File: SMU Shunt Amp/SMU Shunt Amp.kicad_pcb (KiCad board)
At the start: 4 copper layers, 99.1 x 37.6 mm, 51 parts, among them J1 30VDC, J2 Input, J3 Output, U1 LT3088, U2 OPA189IDBVx, U3 THS4021CxDGNx, U4 TLE2426xD, U5 OPA1611AIDR

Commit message: PCB layout initial.
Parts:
- removed C10, C14, C15: 10u, Capacitor_SMD:CP_Elec_6.3x7.7
- removed C11: 1u, Capacitor_SMD:C_0805_2012Metric_Pad1.18x1.45mm_HandSolder
- removed C12, C13: Optional, Capacitor_SMD:C_0805_2012Metric_Pad1.18x1.45mm_HandSolder
- removed JP1: Term, Connector_PinHeader_2.54mm:PinHeader_1x02_P2.54mm_Vertical
- removed JP2: SIG, Connector_PinHeader_2.54mm:PinHeader_1x02_P2.54mm_Vertical
- removed JP3: 100uV, Connector_PinHeader_2.54mm:PinHeader_1x02_P2.54mm_Vertical
- removed JP4: GND, Connector_PinHeader_2.54mm:PinHeader_1x02_P2.54mm_Vertical
- removed R10: 1M, Resistor_SMD:R_0805_2012Metric_Pad1.20x1.40mm_HandSolder
- removed R11: 56K, Resistor_SMD:R_0805_2012Metric_Pad1.20x1.40mm_HandSolder
- removed R12: 1.47K, Resistor_SMD:R_0805_2012Metric_Pad1.20x1.40mm_HandSolder
- removed R13: 0R, Resistor_SMD:R_0805_2012Metric_Pad1.20x1.40mm_HandSolder
- removed R14: 49.9, Resistor_SMD:R_0805_2012Metric_Pad1.20x1.40mm_HandSolder
- removed R15: 1K, Resistor_SMD:R_0805_2012Metric_Pad1.20x1.40mm_HandSolder
- removed TP1: 100uV, TestPoint:TestPoint_Keystone_5010-5014_Multipurpose
- removed TP2: +14V, TestPoint:TestPoint_Keystone_5010-5014_Multipurpose
- removed TP3: -14V, TestPoint:TestPoint_Keystone_5010-5014_Multipurpose
- removed TP4: GND, TestPoint:TestPoint_Keystone_5010-5014_Multipurpose
- removed U3: THS4021CxDGNx, Package_SO:MSOP-8-1EP_3x3mm_P0.65mm_EP1.73x1.85mm_ThermalVias
- removed U4: TLE2426xD, Package_SO:SOIC-8_3.9x4.9mm_P1.27mm
- removed U5: OPA1611AIDR, Package_SO:SOIC-8_3.9x4.9mm_P1.27mm
- added D2: MBRA340, Diode_SMD:D_SMA_Handsoldering, F.Cu at (111.2, 39.9)
- added D3: Vz=30, Diode_SMD:D_SOD-123, F.Cu at (116.0, 50.3)
- C1, C2, C3, C4, R1: moved to B.Cu
- C5, C6: value 100n -> 10u; footprint Capacitor_SMD:C_0805_2012Metric_Pad1.18x1.45mm_HandSolder -> Capacitor_SMD:CP_Elec_6.3x7.7; moved to F.Cu
- C7: value 10u -> 715p; footprint Capacitor_SMD:CP_Elec_6.3x7.7 -> Capacitor_SMD:C_0805_2012Metric_Pad1.18x1.45mm_HandSolder; moved to B.Cu
- C8: value 10u -> Optional; footprint Capacitor_SMD:CP_Elec_6.3x7.7 -> Capacitor_SMD:C_0805_2012Metric_Pad1.18x1.45mm_HandSolder; moved to B.Cu
- C9: value 1u -> 6.8p; moved to B.Cu
- D1: value D -> MBRA340; footprint Diode_SMD:D_SOD-128 -> Diode_SMD:D_SMA_Handsoldering
- J1: footprint TerminalBlock_Phoenix:TerminalBlock_Phoenix_PT-1,5-2-5.0-H_1x02_P5.00mm_Horizontal -> TerminalBlock_Phoenix:TerminalBlock_Phoenix_PT-1,5-3-5.0-H_1x03_P5.00mm_Horizontal
- R2: value 1.54M -> 150R; moved to B.Cu
- R3: value 11R -> 14.7K; moved to B.Cu
- R4: value 560K -> 430R; moved to B.Cu
- R5: value 750R -> 14.7K; moved to B.Cu
- R6: value 0R -> 4.3K; moved to B.Cu
- R7: value 1.47K -> 60.4R; moved to B.Cu
- R8: value 15R -> 604R; moved to B.Cu
- R9: value 0R -> 49.9
- U1: value LT3088 -> OPA189IDBVx; footprint Package_TO_SOT_SMD:SOT-223 -> Package_TO_SOT_SMD:SOT-23-5_HandSoldering; moved to B.Cu
- U2: value OPA189IDBVx -> THS3092D; footprint Package_TO_SOT_SMD:SOT-23-5_HandSoldering -> Package_SO:SOIC-8_3.9x4.9mm_P1.27mm; moved to B.Cu
- moved C9 64.8 mm to (146.3, 47.5), turned to 180 degrees
- moved R5 63.3 mm to (146.3, 49.9)
- moved C7 55.6 mm to (142.9, 48.8), turned to 90 degrees
- moved R4 55.6 mm to (139.1, 55.0)
- moved U1 45.2 mm to (135.0, 52.5)
- moved D1 40.8 mm to (111.2, 60.9)
- moved J1 33.2 mm to (108.7, 45.5)
- moved H4 28.6 mm to (103.5, 65.3)
- moved H3 28.6 mm to (103.5, 35.9)
- moved C6 28.6 mm to (120.3, 43.7)
- moved R1 24.5 mm to (128.9, 51.4), turned to 90 degrees
- moved R2 21.4 mm to (137.8, 48.8), turned to 90 degrees
- moved R3 19.7 mm to (140.3, 48.8), turned to 90 degrees
- moved C5 18.1 mm to (120.3, 57.0), turned to 90 degrees
- moved R8 16.7 mm to (151.8, 53.7), turned to 90 degrees
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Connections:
- C7 pad 2: -15V -> GND
- C8 pad 2: GND -> Net-(C8-Pad2)
- C9 pad 2: -15V -> Net-(C7-Pad1)
- D1 pad 1: Net-(C7-Pad1) -> +15V
- J1 pad 1: Net-(D1-Pad2) -> Net-(D2-Pad1)
- J1 pad 2: -15V -> GND
- J2 pad 1: Net-(J2-Pad1) -> Net-(C8-Pad2)
- R1 pad 2: Net-(JP1-Pad1) -> Net-(C8-Pad2)
- R2 pad 1: +15V -> Net-(C7-Pad1)
- R2 pad 2: Net-(C8-Pad1) -> GND
- R3 pad 1: Net-(C8-Pad1) -> Net-(C7-Pad1)
- R4 pad 1: Net-(C9-Pad1) -> Net-(R4-Pad1)
- R4 pad 2: -15V -> Net-(C8-Pad1)
- R5 pad 1: +15V -> Net-(C9-Pad1)
- R5 pad 2: -15V -> Net-(C7-Pad1)
- R6 pad 1: Net-(C12-Pad2) -> Net-(R6-Pad1)
- R6 pad 2: Net-(C13-Pad1) -> Net-(R4-Pad1)
- R7 pad 1: Net-(C13-Pad1) -> Net-(R7-Pad1)
- R7 pad 2: GND -> Net-(R6-Pad1)
- R8 pad 1: Net-(C13-Pad1) -> Net-(C9-Pad1)
- R8 pad 2: GND -> Net-(R7-Pad1)
- R9 pad 1: Net-(R9-Pad1) -> Net-(J3-Pad1)
- R9 pad 2: Net-(C12-Pad1) -> Net-(C9-Pad1)
- U1 pad 1: Net-(C9-Pad1) -> Net-(C8-Pad1)
- U1 pad 2: +15V -> -15V
- U1 pad 3: Net-(C7-Pad1) -> Net-(C8-Pad2)
- U1 pad 4: +15V -> Net-(C7-Pad1)
- U2 pad 1: Net-(C12-Pad1) -> Net-(R6-Pad1)
- U2 pad 2: -15V -> Net-(R4-Pad1)
- U2 pad 3: Net-(JP2-Pad2) -> GND
- U2 pad 4: Net-(C12-Pad2) -> -15V
- U2 pad 5: +15V -> GND
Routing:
- net +15V: track 154.1 -> 56.0 mm, vias 4 -> 2
- net -15V: track 110.8 -> 56.0 mm, vias 4 -> 2
- net Net-(JP2-Pad2): track 30.3 -> 0.00 mm
- net NULLA: track 27.9 -> 0.00 mm
- net Net-(C13-Pad2): track 24.1 -> 0.00 mm, vias 1 -> 0
- net Net-(C7-Pad1): track 36.0 -> 12.4 mm
- net Net-(J2-Pad1): track 22.8 -> 0.00 mm
- net Net-(C12-Pad1): track 22.6 -> 0.00 mm, vias 1 -> 0
- net Net-(R6-Pad1): track 0.00 -> 15.0 mm, vias 0 -> 2
- net Net-(C13-Pad1): track 13.3 -> 0.00 mm
- net Net-(C8-Pad1): track 20.3 -> 10.4 mm
- net Net-(C9-Pad1): track 6.00 -> 15.1 mm
- net Net-(C8-Pad2): track 0.00 -> 8.14 mm
- net Net-(R4-Pad1): track 0.00 -> 5.82 mm
- net Net-(R7-Pad1): track 0.00 -> 5.73 mm
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- removed copper zone on In1.Cu, net (none)
- removed copper zone on In2.Cu, net (none)
- removed copper zone on F.Cu, net -15V
- removed copper zone on B.Cu, net Net-(U3-Pad9)
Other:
- board size 99.1 x 37.6 mm -> 69.9 x 37.6 mm
- board text added: "+"
- board text added: "-"
- board text added: "±15V MAX"
- board text added: "⏚"
- board text removed: "-V"
- board text removed: "30 VDC"
- board text removed: ">"

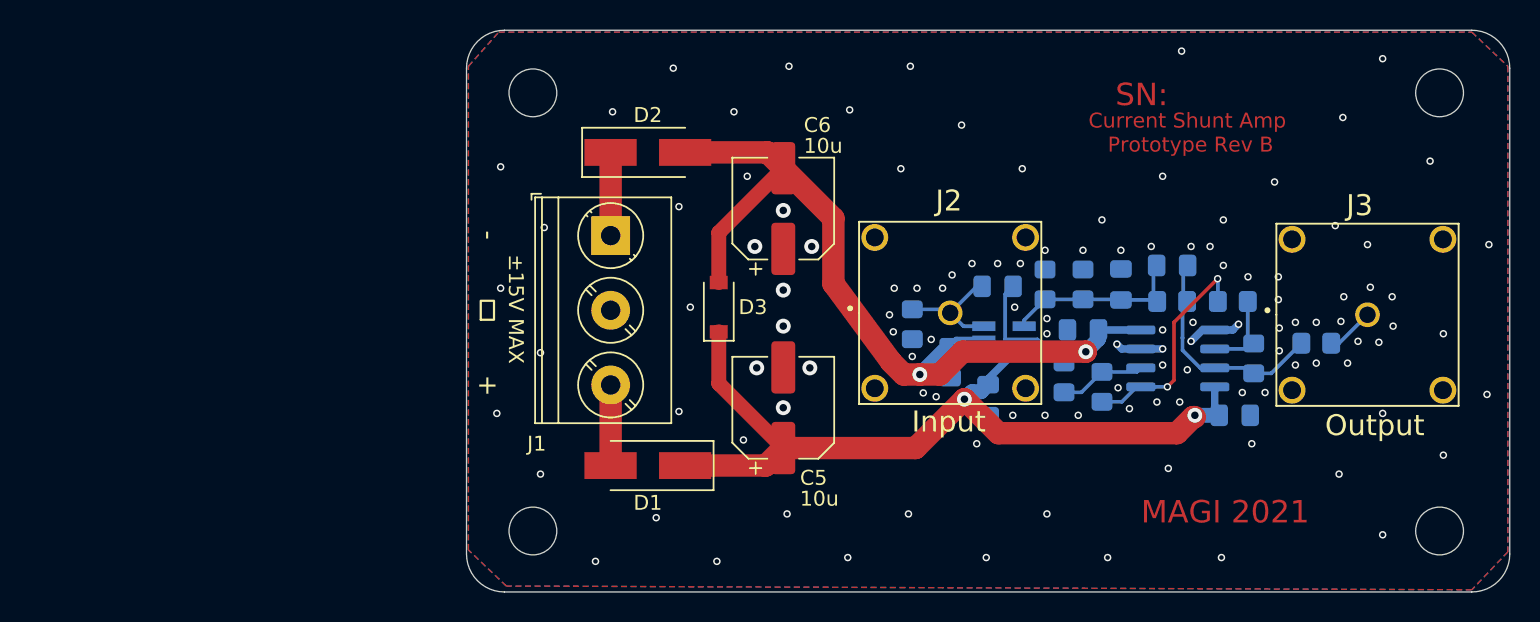
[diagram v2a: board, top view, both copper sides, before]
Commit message: More vias
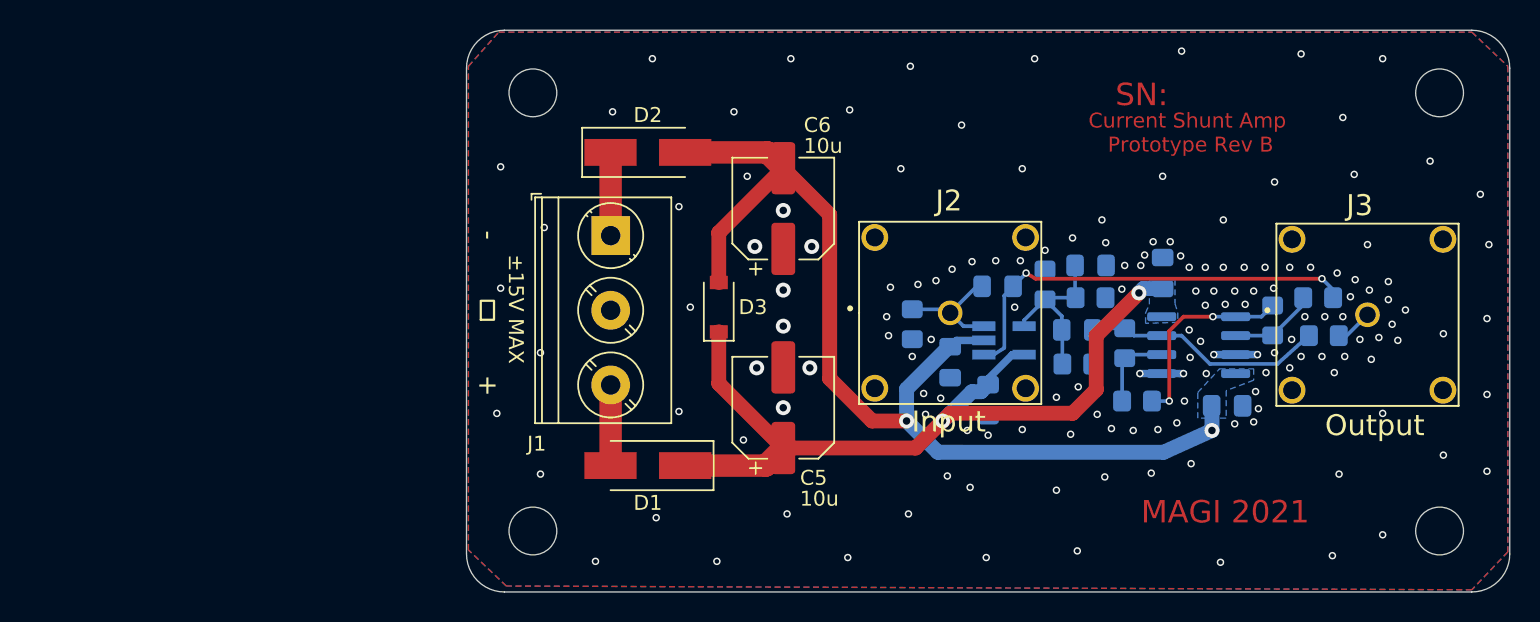
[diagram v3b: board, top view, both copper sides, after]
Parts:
- C8: value Optional -> 1u
- moved R4 17.8 mm to (156.1, 49.7), turned to 0 degrees
- moved R6 12.3 mm to (153.0, 51.2), turned to 270 degrees
- moved C2 10.9 mm to (150.0, 56.9), turned to 180 degrees
- moved C3 10.7 mm to (145.7, 48.0), turned to 90 degrees
- moved R7 9.25 mm to (144.0, 56.6), turned to 0 degrees
- moved R8 8.70 mm to (143.1, 52.7), turned to 270 degrees
- moved C9 7.68 mm to (140.0, 51.8)
- moved R5 7.61 mm to (140.0, 54.1)
- moved C7 2.40 mm to (140.8, 47.5), turned to 0 degrees
- moved U2 1.66 mm to (148.1, 52.8), turned to 180 degrees
- moved R3 1.02 mm to (140.8, 49.7), turned to 0 degrees
- moved R9 0.72 mm to (156.5, 52.2)
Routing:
- net Net-(C8-Pad1): track 10.4 -> 28.6 mm, vias 0 -> 2
- net -15V: track 56.0 -> 70.1 mm
- net Net-(C9-Pad1): track 15.1 -> 18.6 mm
- net Net-(R6-Pad1): track 15.0 -> 13.5 mm
- net GND: track 6.84 -> 5.84 mm, vias 115 -> 153
- net Net-(C7-Pad1): track 12.4 -> 11.5 mm
- net Net-(J3-Pad1): track 3.22 -> 2.50 mm
- added copper zone on B.Cu, net +15V
- added copper zone on B.Cu, net -15V

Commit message: Thicken output paths, add ferrites.
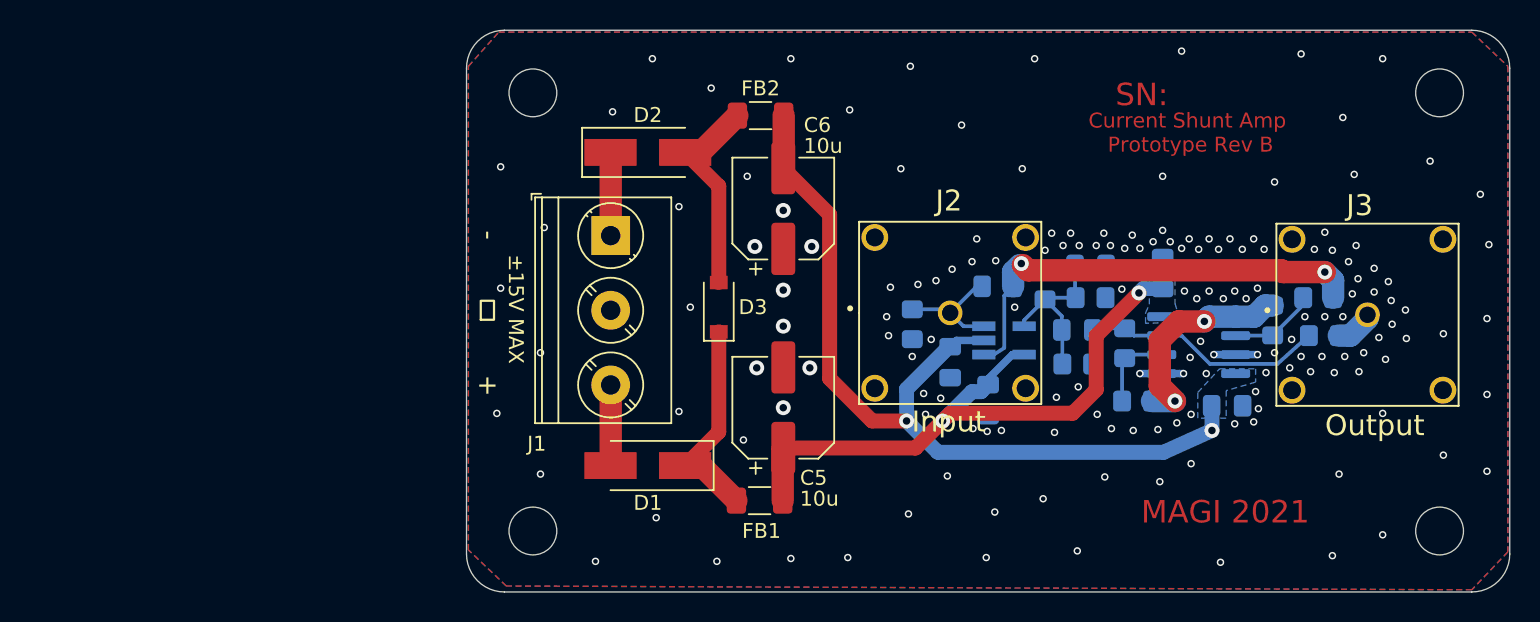
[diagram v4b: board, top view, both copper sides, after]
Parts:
- added FB1: 80R @ 100MHz, Resistor_SMD:R_1206_3216Metric_Pad1.30x1.75mm_HandSolder, F.Cu at (118.7, 63.2)
- added FB2: 80R @ 100MHz, Resistor_SMD:R_1206_3216Metric_Pad1.30x1.75mm_HandSolder, F.Cu at (118.7, 37.5)
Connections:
- D1 pad 1: +15V -> Net-(D1-Pad1)
- D2 pad 2: -15V -> Net-(D2-Pad2)
- D3 pad 1: +15V -> Net-(D1-Pad1)
- D3 pad 2: -15V -> Net-(D2-Pad2)
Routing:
- net Net-(D1-Pad1): track 0.00 -> 14.3 mm
- net Net-(D2-Pad2): track 0.00 -> 14.2 mm
- net +15V: track 56.1 -> 43.0 mm
- net -15V: track 70.1 -> 57.2 mm
- net Net-(C8-Pad1): track 28.6 -> 29.8 mm
- net Net-(R6-Pad1): track 13.5 -> 14.5 mm
- net GND: vias 153 -> 162

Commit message: New layout for better signal integrity
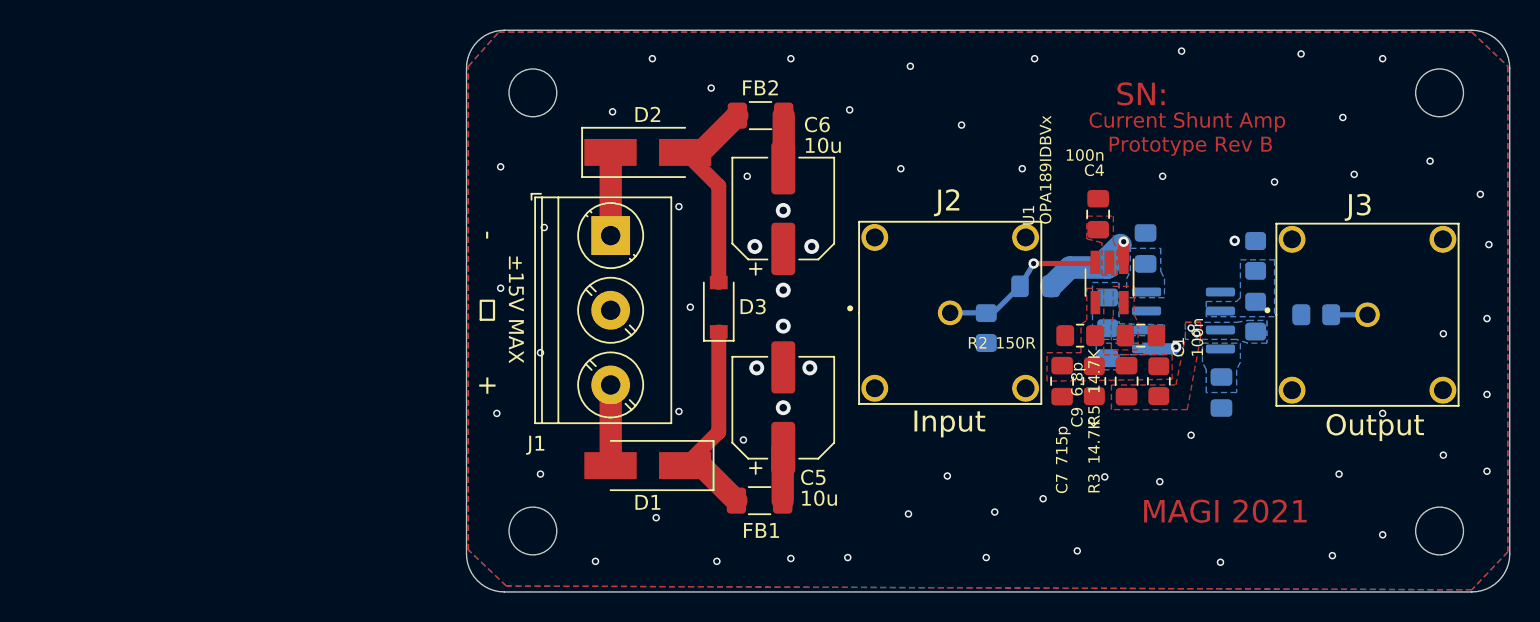
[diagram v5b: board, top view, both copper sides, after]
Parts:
- C1, C4, C7, C9, R2, R3, R5, U1: moved to F.Cu
- moved R4 14.1 mm to (142.0, 48.6), turned to 90 degrees
- moved C4 14.0 mm to (141.4, 44.1), turned to 270 degrees
- moved R7 12.5 mm to (151.9, 46.9), turned to 90 degrees
- moved C2 11.9 mm to (144.5, 46.4), turned to 270 degrees
- moved R6 11.2 mm to (142.0, 52.7), turned to 90 degrees
- moved C1 11.1 mm to (144.2, 52.2), turned to 0 degrees
- moved R8 8.94 mm to (151.9, 50.9), turned to 90 degrees
- moved C3 8.92 mm to (149.6, 56.0), turned to 270 degrees
- moved U1 8.06 mm to (142.1, 48.6), turned to 270 degrees
- moved C7 7.98 mm to (138.9, 55.2), turned to 270 degrees
- moved R3 5.59 mm to (141.1, 55.2), turned to 270 degrees
- moved R5 5.58 mm to (145.4, 55.2), turned to 90 degrees
- moved R1 4.96 mm to (133.9, 51.7)
- moved C9 4.76 mm to (143.3, 55.2), turned to 90 degrees
- moved R2 4.16 mm to (140.1, 52.2), turned to 180 degrees
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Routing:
- net -15V: track 57.2 -> 3.53 mm, vias 2 -> 1
- net +15V: track 43.0 -> 3.54 mm, vias 2 -> 0
- net Net-(C8-Pad1): track 29.8 -> 7.57 mm, vias 2 -> 1
- net Net-(C9-Pad1): track 18.6 -> 0.00 mm, vias 0 -> 2
- net Net-(R6-Pad1): track 14.5 -> 2.02 mm
- net Net-(C7-Pad1): track 11.5 -> 0.00 mm
- net Net-(R4-Pad1): track 5.86 -> 0.00 mm
- net GND: track 5.84 -> 0.00 mm, vias 162 -> 62
- net Net-(R7-Pad1): track 5.70 -> 0.00 mm
- net Net-(C8-Pad2): track 8.14 -> 11.4 mm, vias 0 -> 1
- added copper zone on F.Cu, net +15V
- added copper zone on F.Cu, net -15V
- added copper zone on F.Cu, net Net-(C7-Pad1)
- added copper zone on B.Cu, net Net-(C9-Pad1)
- added copper zone on F.Cu, net Net-(C9-Pad1)
- added copper zone on B.Cu, net Net-(R4-Pad1)
- added copper zone on B.Cu, net Net-(R6-Pad1)
- added copper zone on B.Cu, net Net-(R7-Pad1)

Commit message: Most routing done.
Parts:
- moved C1 3.89 mm to (147.4, 50.0)
- moved C2 2.69 mm to (147.1, 47.2), turned to 180 degrees
- moved C8 2.68 mm to (139.8, 48.6), turned to 270 degrees
- moved C4 1.52 mm to (142.9, 44.1)
- moved C7 1.52 mm to (140.5, 55.2)
- moved C9 1.52 mm to (144.8, 55.2)
- moved R2 1.52 mm to (141.7, 52.2)
- moved R3 1.52 mm to (142.6, 55.2)
- moved R5 1.52 mm to (146.9, 55.2)
- moved U1 1.52 mm to (143.6, 48.6)
- moved R1 1.14 mm to (134.4, 50.7)
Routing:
- net Net-(C8-Pad2): track 11.4 -> 0.00 mm, vias 1 -> 2
- net Net-(C9-Pad1): track 0.00 -> 11.2 mm
- net +15V: track 3.54 -> 13.8 mm, vias 0 -> 10
- net Net-(R6-Pad1): track 2.02 -> 10.6 mm, vias 2 -> 3
- net Net-(C8-Pad1): track 7.57 -> 1.34 mm, vias 1 -> 4
- net Net-(D2-Pad1): track 5.58 -> 0.00 mm
- net Net-(D1-Pad2): track 5.40 -> 0.00 mm
- net Net-(D1-Pad1): track 14.3 -> 15.3 mm
- net Net-(D2-Pad2): track 14.2 -> 15.1 mm
- net -15V: track 3.53 -> 3.94 mm, vias 1 -> 10
- net GND: vias 62 -> 65
- added copper zone on In1.Cu, net +15V
- added copper zone on In1.Cu, net -15V
- added copper zone on B.Cu, net Net-(C8-Pad1)
- added copper zone on In1.Cu, net Net-(C8-Pad1)
- added copper zone on B.Cu, net Net-(C8-Pad2)
- added copper zone on F.Cu, net Net-(C8-Pad2)
- added copper zone on F.Cu, net Net-(D1-Pad2)
- added copper zone on F.Cu, net Net-(D2-Pad1)
- removed copper zone on F.Cu, net Net-(C9-Pad1)

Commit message: Before *big* OPA189 move.
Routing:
- net Net-(R6-Pad1): track 10.6 -> 0.00 mm
- net +15V: track 13.8 -> 5.74 mm
- net Net-(C8-Pad1): track 1.34 -> 0.00 mm, vias 4 -> 5
- net GND: vias 65 -> 66
- added copper zone on F.Cu, net Net-(C8-Pad1)

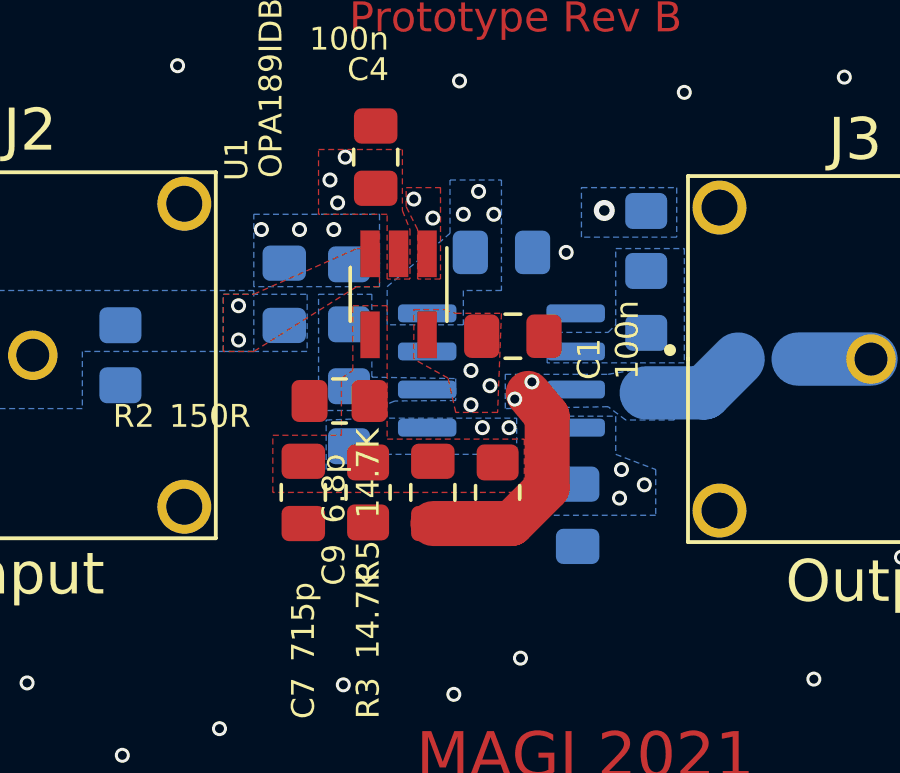
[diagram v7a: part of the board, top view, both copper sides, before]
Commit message: Rollback 189 move, tighten FB path, improve power routing.
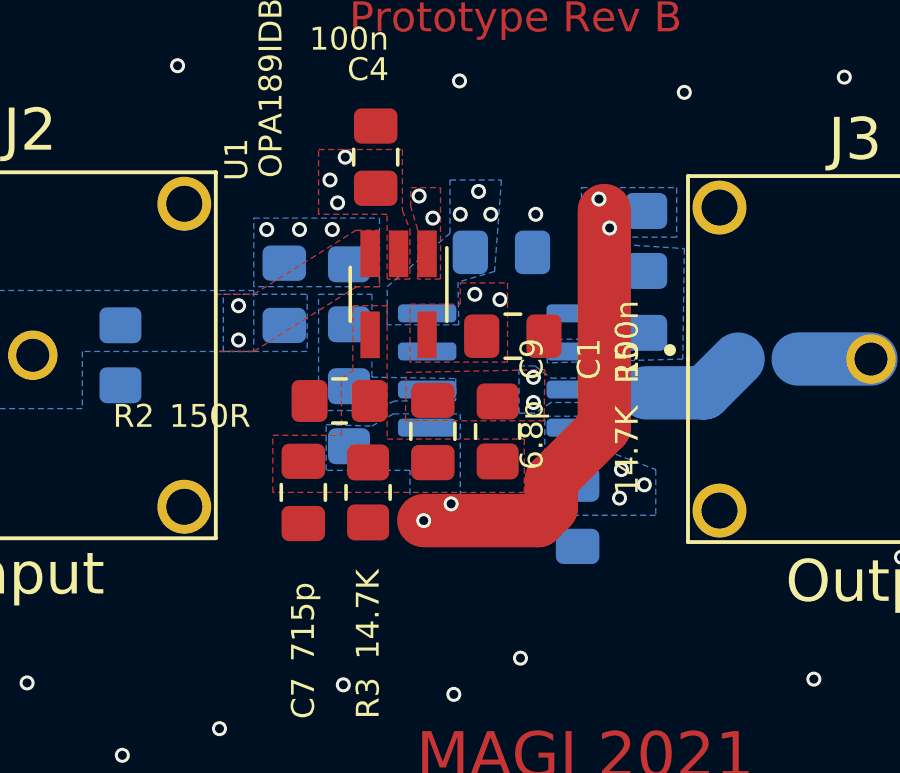
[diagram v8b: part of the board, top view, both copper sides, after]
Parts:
- moved C9 2.03 mm to (144.8, 53.2), turned to 270 degrees
- moved R5 2.03 mm to (146.9, 53.2), turned to 270 degrees
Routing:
- net Net-(R6-Pad1): track 0.00 -> 15.1 mm, vias 3 -> 4
- net Net-(C9-Pad1): track 11.2 -> 3.53 mm
- net +15V: track 5.74 -> 0.00 mm, vias 10 -> 9
- net -15V: track 3.94 -> 0.00 mm
- added copper zone on F.Cu, net Net-(C9-Pad1)
